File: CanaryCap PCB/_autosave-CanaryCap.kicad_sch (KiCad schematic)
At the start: 3 parts, among them U1 ESP32-C6-MINI-1, U2 TPS5431DDA, U3 LM3940 3.3V-SOT223

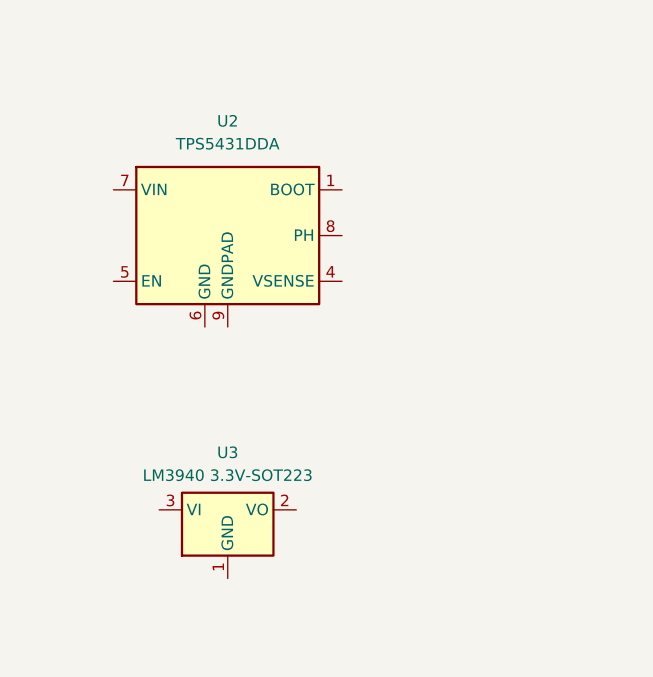
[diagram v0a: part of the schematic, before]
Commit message: Started some basic board definition and component selection DO NOT USE LAYOUT
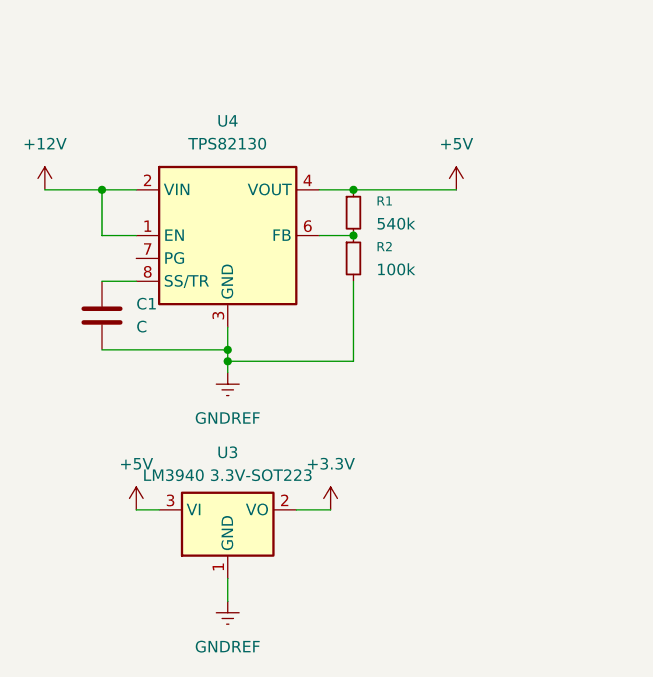
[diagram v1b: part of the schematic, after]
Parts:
- removed U2: TPS5431DDA, Package_SO:TI_SO-PowerPAD-8_ThermalVias, symbol Regulator_Switching:TPS5431DDA
- added C1: C, Capacitor_SMD:C_0603_1608Metric_Pad1.08x0.95mm_HandSolder, symbol Device:C
- added R1: 540k, Resistor_SMD:R_0603_1608Metric_Pad0.98x0.95mm_HandSolder, symbol Device:R_Small
- added R2: 100k, Resistor_SMD:R_0603_1608Metric_Pad0.98x0.95mm_HandSolder, symbol Device:R_Small
- added U4: TPS82130, Package_LGA:Texas_SIL0008D_MicroSiP-8-1EP_2.8x3mm_P0.65mm_EP1.1x1.9mm_ThermalVias, symbol Regulator_Switching:TPS82130
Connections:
- net GNDREF: now also U3.1 (GND), C1.2, R2.2, U4.3 (GND), U4.9 (GND)
- net +3.3V: now reaches U3.2 (VO)
- net +5V: now reaches U3.3 (VI)
- net +5V: now also R1.1, U4.4 (VOUT), U4.5 (VOUT)
- new net: R1.2, R2.1, U4.6 (FB)
- new net: C1.1, U4.8 (SS/TR)
- new net +12V: U4.1 (EN), U4.2 (VIN)
